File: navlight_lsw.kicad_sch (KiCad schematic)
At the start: 7 parts, among them U13 TPS26400PWP

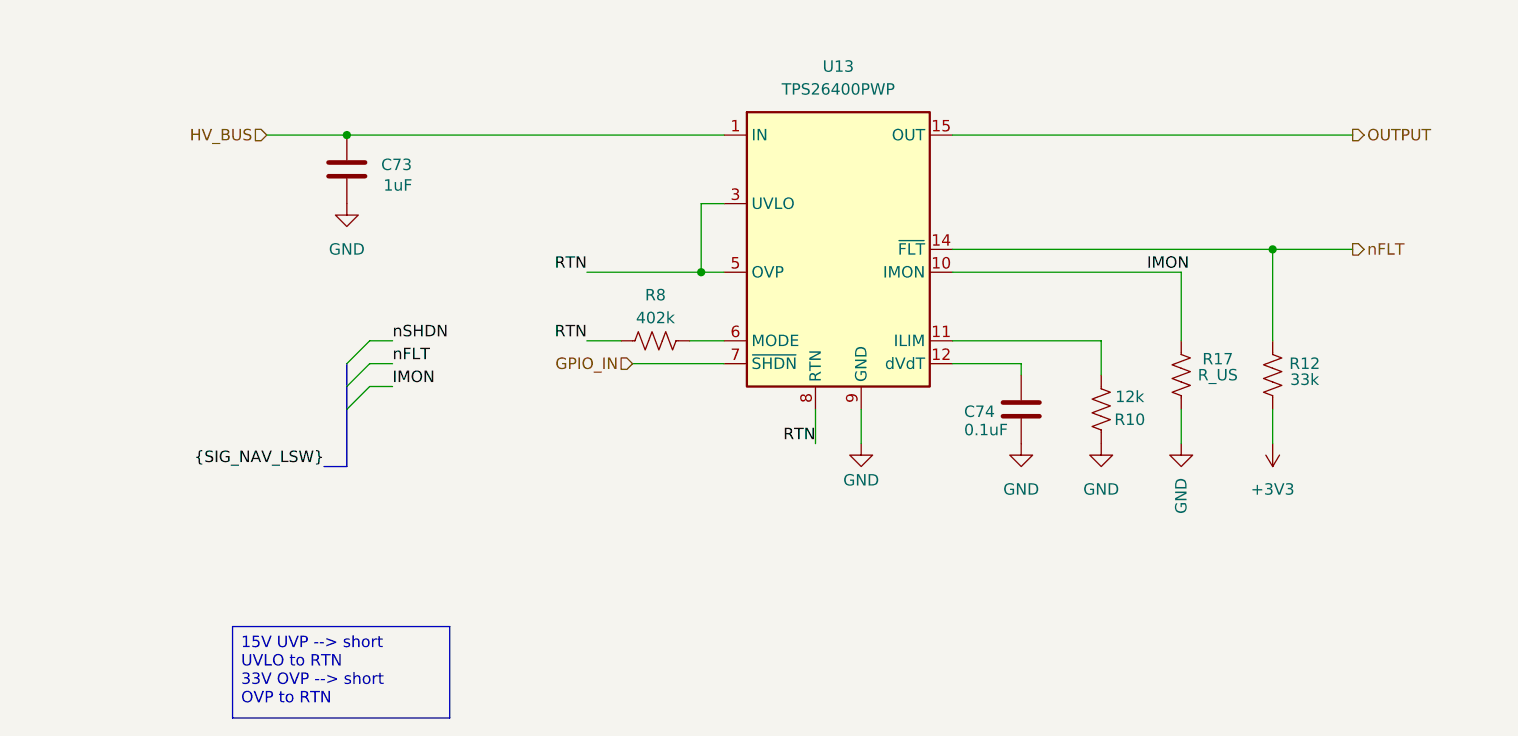
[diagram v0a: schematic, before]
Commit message: Starting bus load switch layout
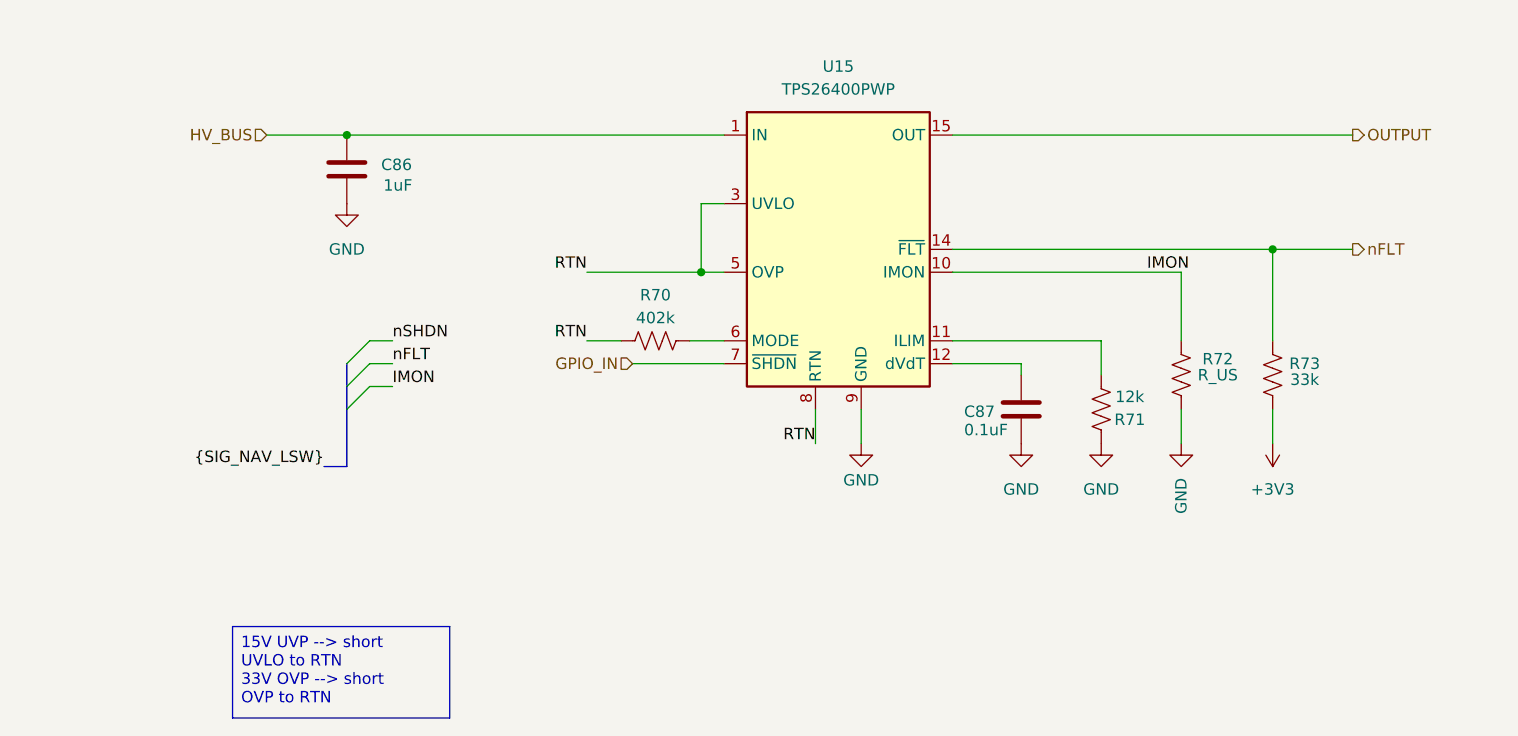
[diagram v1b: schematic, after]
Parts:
- renumbered C73 to C86, C74 to C87, R8 to R70, R10 to R71, R17 to R72, R12 to R73, U13 to U15
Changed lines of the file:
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@@
 		(on_board yes)
 		(dnp no)
-		(property "Reference" "C74"
+		(property "Reference" "C87"
 			(at 166.37 119.634 0)
 			(effects
@@
 			(project "PowerBoard"
 				(path "/99785679-20de-4827-b4cc-bc3c187068c9/9564929a-642e-4163-88c2-45054b63a5ed/a2a5e176-2ba3-4f1c-82d3-fb6903dd7d61"
-					(reference "C74")
+					(reference "C89")
 					(unit 1)
 				)
 				(path "/99785679-20de-4827-b4cc-bc3c187068c9/9564929a-642e-4163-88c2-45054b63a5ed/dd15ba19-6ae0-43ad-9da3-66d2cc4e2bc8"
-					(reference "C74")
+					(reference "C87")
 					(unit 1)
 				)
@@
 		(on_board yes)
 		(dnp no)
-		(property "Reference" "R8"
+		(property "Reference" "R70"
 			(at 132.08 106.68 90)
 			(effects
@@
 			(project ""
 				(path "/99785679-20de-4827-b4cc-bc3c187068c9/9564929a-642e-4163-88c2-45054b63a5ed/a2a5e176-2ba3-4f1c-82d3-fb6903dd7d61"
-					(reference "R9")
+					(reference "R74")
 					(unit 1)
 				)
 				(path "/99785679-20de-4827-b4cc-bc3c187068c9/9564929a-642e-4163-88c2-45054b63a5ed/dd15ba19-6ae0-43ad-9da3-66d2cc4e2bc8"
-					(reference "R8")
+					(reference "R70")
 					(unit 1)
 				)
@@
 		(dnp no)
 		(fields_autoplaced yes)
-		(property "Reference" "#PWR0120"
+		(property "Reference" "#PWR0152"
 			(at 97.79 102.87 0)
 			(effects
@@
 			(project "PowerBoard"
 				(path "/99785679-20de-4827-b4cc-bc3c187068c9/9564929a-642e-4163-88c2-45054b63a5ed/a2a5e176-2ba3-4f1c-82d3-fb6903dd7d61"
-					(reference "#PWR0120")
+					(reference "#PWR0158")
 					(unit 1)
 				)
 				(path "/99785679-20de-4827-b4cc-bc3c187068c9/9564929a-642e-4163-88c2-45054b63a5ed/dd15ba19-6ae0-43ad-9da3-66d2cc4e2bc8"
-					(reference "#PWR0120")
+					(reference "#PWR0152")
 					(unit 1)
 				)
@@
 		(dnp no)
 		(fields_autoplaced yes)
-		(property "Reference" "#PWR028"
+		(property "Reference" "#PWR0154"
 			(at 172.72 129.54 0)
 			(effects
@@
 			(project ""
 				(path "/99785679-20de-4827-b4cc-bc3c187068c9/9564929a-642e-4163-88c2-45054b63a5ed/a2a5e176-2ba3-4f1c-82d3-fb6903dd7d61"
-					(reference "#PWR029")
+					(reference "#PWR0160")
 					(unit 1)
 				)
 				(path "/99785679-20de-4827-b4cc-bc3c187068c9/9564929a-642e-4163-88c2-45054b63a5ed/dd15ba19-6ae0-43ad-9da3-66d2cc4e2bc8"
-					(reference "#PWR028")
+					(reference "#PWR0154")
 					(unit 1)
 				)
@@
 		(dnp no)
 		(fields_autoplaced yes)
-		(property "Reference" "#PWR034"
+		(property "Reference" "#PWR0157"
 			(at 200.66 119.38 0)
 			(effects
@@
 			(project ""
 				(path "/99785679-20de-4827-b4cc-bc3c187068c9/9564929a-642e-4163-88c2-45054b63a5ed/a2a5e176-2ba3-4f1c-82d3-fb6903dd7d61"
-					(reference "#PWR035")
+					(reference "#PWR0163")
 					(unit 1)
 				)
 				(path "/99785679-20de-4827-b4cc-bc3c187068c9/9564929a-642e-4163-88c2-45054b63a5ed/dd15ba19-6ae0-43ad-9da3-66d2cc4e2bc8"
-					(reference "#PWR034")
+					(reference "#PWR0157")
 					(unit 1)
 				)
@@
 		(on_board yes)
 		(dnp no)
-		(property "Reference" "C73"
+		(property "Reference" "C86"
 			(at 101.6 92.202 0)
 			(effects
@@
 			(project "PowerBoard"
 				(path "/99785679-20de-4827-b4cc-bc3c187068c9/9564929a-642e-4163-88c2-45054b63a5ed/a2a5e176-2ba3-4f1c-82d3-fb6903dd7d61"
-					(reference "C73")
+					(reference "C88")
 					(unit 1)
 				)
 				(path "/99785679-20de-4827-b4cc-bc3c187068c9/9564929a-642e-4163-88c2-45054b63a5ed/dd15ba19-6ae0-43ad-9da3-66d2cc4e2bc8"
-					(reference "C73")
+					(reference "C86")
 					(unit 1)
 				)
@@
 		(on_board yes)
 		(dnp no)
-		(property "Reference" "#PWR0121"
+		(property "Reference" "#PWR0153"
 			(at 154.94 129.54 0)
 			(effects
@@
 			(project "PowerBoard"
 				(path "/99785679-20de-4827-b4cc-bc3c187068c9/9564929a-642e-4163-88c2-45054b63a5ed/a2a5e176-2ba3-4f1c-82d3-fb6903dd7d61"
-					(reference "#PWR0121")
+					(reference "#PWR0159")
 					(unit 1)
 				)
 				(path "/99785679-20de-4827-b4cc-bc3c187068c9/9564929a-642e-4163-88c2-45054b63a5ed/dd15ba19-6ae0-43ad-9da3-66d2cc4e2bc8"
-					(reference "#PWR0121")
+					(reference "#PWR0153")
 					(unit 1)
 				)
@@
 		(dnp no)
 		(fields_autoplaced yes)
-		(property "Reference" "#PWR030"
+		(property "Reference" "#PWR0155"
 			(at 181.61 129.54 0)
 			(effects
@@
 			(project "PowerBoard"
 				(path "/99785679-20de-4827-b4cc-bc3c187068c9/9564929a-642e-4163-88c2-45054b63a5ed/a2a5e176-2ba3-4f1c-82d3-fb6903dd7d61"
-					(reference "#PWR031")
+					(reference "#PWR0161")
 					(unit 1)
 				)
 				(path "/99785679-20de-4827-b4cc-bc3c187068c9/9564929a-642e-4163-88c2-45054b63a5ed/dd15ba19-6ae0-43ad-9da3-66d2cc4e2bc8"
-					(reference "#PWR030")
+					(reference "#PWR0155")
 					(unit 1)
 				)
@@
 		(on_board yes)
 		(dnp no)
-		(property "Reference" "R17"
+		(property "Reference" "R72"
 			(at 194.564 113.792 0)
 			(effects
@@
 			(project ""
 				(path "/99785679-20de-4827-b4cc-bc3c187068c9/9564929a-642e-4163-88c2-45054b63a5ed/a2a5e176-2ba3-4f1c-82d3-fb6903dd7d61"
-					(reference "R18")
+					(reference "R76")
 					(unit 1)
 				)
 				(path "/99785679-20de-4827-b4cc-bc3c187068c9/9564929a-642e-4163-88c2-45054b63a5ed/dd15ba19-6ae0-43ad-9da3-66d2cc4e2bc8"
-					(reference "R17")
+					(reference "R72")
 					(unit 1)
 				)
@@
 		(dnp no)
 		(fields_autoplaced yes)
-		(property "Reference" "U13"
+		(property "Reference" "U15"
 			(at 152.4 81.28 0)
 			(effects
@@
 			(project "PowerBoard"
 				(path "/99785679-20de-4827-b4cc-bc3c187068c9/9564929a-642e-4163-88c2-45054b63a5ed/a2a5e176-2ba3-4f1c-82d3-fb6903dd7d61"
-					(reference "U13")
+					(reference "U16")
 					(unit 1)
 				)
 				(path "/99785679-20de-4827-b4cc-bc3c187068c9/9564929a-642e-4163-88c2-45054b63a5ed/dd15ba19-6ae0-43ad-9da3-66d2cc4e2bc8"
-					(reference "U13")
+					(reference "U15")
 					(unit 1)
 				)
@@
 		(on_board yes)
 		(dnp no)
-		(property "Reference" "R10"
+		(property "Reference" "R71"
 			(at 184.785 120.523 0)
 			(effects
@@
 			(project ""
 				(path "/99785679-20de-4827-b4cc-bc3c187068c9/9564929a-642e-4163-88c2-45054b63a5ed/a2a5e176-2ba3-4f1c-82d3-fb6903dd7d61"
-					(reference "R11")
+					(reference "R75")
 					(unit 1)
 				)
 				(path "/99785679-20de-4827-b4cc-bc3c187068c9/9564929a-642e-4163-88c2-45054b63a5ed/dd15ba19-6ae0-43ad-9da3-66d2cc4e2bc8"
-					(reference "R10")
+					(reference "R71")
 					(unit 1)
 				)
@@
 		(on_board yes)
 		(dnp no)
-		(property "Reference" "R12"
+		(property "Reference" "R73"
 			(at 204.216 114.3 0)
 			(effects
@@
 			(project "PowerBoard"
 				(path "/99785679-20de-4827-b4cc-bc3c187068c9/9564929a-642e-4163-88c2-45054b63a5ed/a2a5e176-2ba3-4f1c-82d3-fb6903dd7d61"
-					(reference "R13")
+					(reference "R77")
 					(unit 1)
 				)
 				(path "/99785679-20de-4827-b4cc-bc3c187068c9/9564929a-642e-4163-88c2-45054b63a5ed/dd15ba19-6ae0-43ad-9da3-66d2cc4e2bc8"
-					(reference "R12")
+					(reference "R73")
 					(unit 1)
 				)
@@
 		(dnp no)
 		(fields_autoplaced yes)
-		(property "Reference" "#PWR032"
+		(property "Reference" "#PWR0156"
 			(at 190.5 129.54 0)
 			(effects
@@
 			(project "PowerBoard"
 				(path "/99785679-20de-4827-b4cc-bc3c187068c9/9564929a-642e-4163-88c2-45054b63a5ed/a2a5e176-2ba3-4f1c-82d3-fb6903dd7d61"
-					(reference "#PWR033")
+					(reference "#PWR0162")
 					(unit 1)
 				)
 				(path "/99785679-20de-4827-b4cc-bc3c187068c9/9564929a-642e-4163-88c2-45054b63a5ed/dd15ba19-6ae0-43ad-9da3-66d2cc4e2bc8"
-					(reference "#PWR032")
-					(unit 1)
-				)
+					(reference "#PWR0156")
+					(unit 1)
+				)

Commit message: Working on it
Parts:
- removed R70: 402k, Resistor_SMD:R_0603_1608Metric, symbol Device:R_US
- removed R71: 12k, Resistor_SMD:R_0603_1608Metric, symbol Device:R_US
- removed R72: R_US, Resistor_SMD:R_0603_1608Metric, symbol Device:R_US
- removed R73: 33k, Resistor_SMD:R_0603_1608Metric, symbol Device:R_US
- removed U15: TPS26400PWP, Package_DFN_QFN:VQFN-24-1EP_4x4mm_P0.5mm_EP2.45x2.45mm_ThermalVias, symbol Power_Management:TPS26400PWP
- added R66: 402k, Resistor_SMD:R_0603_1608Metric, symbol Device:R_US
- added R67: 33k, Resistor_SMD:R_0603_1608Metric, symbol Device:R_US
- added R68, R69: 12k, Resistor_SMD:R_0603_1608Metric, symbol Device:R_US
- added U15: TPS26400RHFR, _PowerBoard:RHF0024A-MFG, symbol _TPS26400RHFR:TPS26400RHFR
- C87: Supplier_2 (none) -> JLCPCB; Supplier_2_Price @ QTY (none) -> 1
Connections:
- net +3V3: now also R67.1
- net GND: now also U15.17 (GND); no longer C87.2
- net GPIO_IN: now also U15.14 (SHDN_N)
- net HV_BUS: now also U15.8 (IN), U15.9 (IN)
- net OUTPUT: now also U15.23 (OUT), U15.24 (OUT)
- net RTN: now also C87.1, R66.1, R68.1, R69.1, U15.10 (UVLO), U15.12 (OVP), U15.15 (RTN), U15.25 (PowerPAD)
- net nFLT: now also R67.2, U15.22 (FLT_N)
- new net: R69.2, U15.19 (ILIM)
- new net: R66.2, U15.13 (MODE)
- new net: C87.2, U15.20 (dVdT)
- new net: R68.2, U15.18 (IMON)
- no-connect marks 0 -> 10

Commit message: Working on schematic and layout
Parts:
- renumbered R66 to R67, R67 to R68, R68 to R69, R69 to R70, U15 to U16
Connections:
- net GPIO_IN is gone; now on net nSHDN: U16.14 (SHDN_N)
- net IMON: now also R69.2, U16.18 (IMON)
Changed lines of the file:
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@@
+		)
+	)
+	(label "nSHDN"
+		(at 193.04 102.87 0)
+		(effects
+			(font
+				(size 1.27 1.27)
+			)
+			(justify left bottom)
+		)
+	)
+	(label "IMON"
+		(at 172.72 107.95 0)
+		(effects
+			(font
+				(size 1.27 1.27)
+			)
+			(justify left bottom)
 		)
 	)
@@
 		)
 	)
+	(label "nFLT"
+		(at 175.26 93.98 0)
+		(effects
+			(font
+				(size 1.27 1.27)
+			)
+			(justify left bottom)
+		)
+	)
 	(label "nSHDN"
 		(at 87.63 111.76 0)
@@
 			)
 			(justify left bottom)
-		)
-	)
-	(label "{SIG_NAV_LSW}"
-		(at 80.01 125.73 180)
-		(effects
-			(font
-				(size 1.27 1.27)
-			)
-			(justify right bottom)
 		)
 	)
@@
 		)
 	)
-	(hierarchical_label "GPIO_IN"
-		(shape input)
-		(at 193.04 102.87 0)
+	(hierarchical_label "{SIG_NAV_LSW}"
+		(shape bidirectional)
+		(at 80.01 125.73 180)
 		(effects
 			(font
 				(size 1.27 1.27)
 			)
-			(justify left)
-		)
-	)
-	(hierarchical_label "nFLT"
-		(shape output)
-		(at 175.26 93.98 0)
-		(effects
-			(font
-				(size 1.27 1.27)
-			)
-			(justify left)
+			(justify right)
 		)
 	)
@@
 		(on_board yes)
 		(dnp no)
-		(property "Reference" "R69"
-			(at 181.61 108.712 90)
+		(property "Reference" "R70"
+			(at 181.61 109.728 90)
 			(effects
 				(font
@@
 			(project "PowerBoard"
 				(path "/99785679-20de-4827-b4cc-bc3c187068c9/9564929a-642e-4163-88c2-45054b63a5ed/a2a5e176-2ba3-4f1c-82d3-fb6903dd7d61"
-					(reference "R73")
+					(reference "R74")
 					(unit 1)
 				)
 				(path "/99785679-20de-4827-b4cc-bc3c187068c9/9564929a-642e-4163-88c2-45054b63a5ed/dd15ba19-6ae0-43ad-9da3-66d2cc4e2bc8"
-					(reference "R69")
+					(reference "R70")
 					(unit 1)
 				)
@@
 		(on_board yes)
 		(dnp no)
-		(property "Reference" "R66"
+		(property "Reference" "R67"
 			(at 119.38 102.87 90)
 			(effects
@@
 			(project "PowerBoard"
 				(path "/99785679-20de-4827-b4cc-bc3c187068c9/9564929a-642e-4163-88c2-45054b63a5ed/a2a5e176-2ba3-4f1c-82d3-fb6903dd7d61"
-					(reference "R70")
+					(reference "R71")
 					(unit 1)
 				)
 				(path "/99785679-20de-4827-b4cc-bc3c187068c9/9564929a-642e-4163-88c2-45054b63a5ed/dd15ba19-6ae0-43ad-9da3-66d2cc4e2bc8"
-					(reference "R66")
+					(reference "R67")
 					(unit 1)
 				)
@@
 		(on_board yes)
 		(dnp no)
-		(property "Reference" "R67"
+		(property "Reference" "R68"
 			(at 185.42 94.742 90)
 			(effects
@@
 			(project "PowerBoard"
 				(path "/99785679-20de-4827-b4cc-bc3c187068c9/9564929a-642e-4163-88c2-45054b63a5ed/a2a5e176-2ba3-4f1c-82d3-fb6903dd7d61"
-					(reference "R71")
+					(reference "R72")
 					(unit 1)
 				)
 				(path "/99785679-20de-4827-b4cc-bc3c187068c9/9564929a-642e-4163-88c2-45054b63a5ed/dd15ba19-6ae0-43ad-9da3-66d2cc4e2bc8"
-					(reference "R67")
+					(reference "R68")
 					(unit 1)
 				)
@@
 		(dnp no)
 		(fields_autoplaced yes)
-		(property "Reference" "#PWR0152"
+		(property "Reference" "#PWR0155"
 			(at 82.55 101.6 0)
 			(effects
@@
 			(project "PowerBoard"
 				(path "/99785679-20de-4827-b4cc-bc3c187068c9/9564929a-642e-4163-88c2-45054b63a5ed/a2a5e176-2ba3-4f1c-82d3-fb6903dd7d61"
+					(reference "#PWR0158")
+					(unit 1)
+				)
+				(path "/99785679-20de-4827-b4cc-bc3c187068c9/9564929a-642e-4163-88c2-45054b63a5ed/dd15ba19-6ae0-43ad-9da3-66d2cc4e2bc8"
 					(reference "#PWR0155")
-					(unit 1)
-				)
-				(path "/99785679-20de-4827-b4cc-bc3c187068c9/9564929a-642e-4163-88c2-45054b63a5ed/dd15ba19-6ae0-43ad-9da3-66d2cc4e2bc8"
-					(reference "#PWR0152")
 					(unit 1)
 				)
@@
 		(on_board yes)
 		(dnp no)
-		(property "Reference" "#PWR0153"
+		(property "Reference" "#PWR0156"
 			(at 177.8 133.35 0)
 			(effects
@@
 			(project "PowerBoard"
 				(path "/99785679-20de-4827-b4cc-bc3c187068c9/9564929a-642e-4163-88c2-45054b63a5ed/a2a5e176-2ba3-4f1c-82d3-fb6903dd7d61"
+					(reference "#PWR0159")
+					(unit 1)
+				)
+				(path "/99785679-20de-4827-b4cc-bc3c187068c9/9564929a-642e-4163-88c2-45054b63a5ed/dd15ba19-6ae0-43ad-9da3-66d2cc4e2bc8"
 					(reference "#PWR0156")
-					(unit 1)
-				)
-				(path "/99785679-20de-4827-b4cc-bc3c187068c9/9564929a-642e-4163-88c2-45054b63a5ed/dd15ba19-6ae0-43ad-9da3-66d2cc4e2bc8"
-					(reference "#PWR0153")
 					(unit 1)
 				)
@@
 		(dnp no)
 		(fields_autoplaced yes)
-		(property "Reference" "U15"
+		(property "Reference" "U16"
 			(at 151.13 77.47 0)
 			(effects
@@
 			(project ""
 				(path "/99785679-20de-4827-b4cc-bc3c187068c9/9564929a-642e-4163-88c2-45054b63a5ed/a2a5e176-2ba3-4f1c-82d3-fb6903dd7d61"
+					(reference "U17")
+					(unit 1)
+				)
+				(path "/99785679-20de-4827-b4cc-bc3c187068c9/9564929a-642e-4163-88c2-45054b63a5ed/dd15ba19-6ae0-43ad-9da3-66d2cc4e2bc8"
 					(reference "U16")
-					(unit 1)
-				)
-				(path "/99785679-20de-4827-b4cc-bc3c187068c9/9564929a-642e-4163-88c2-45054b63a5ed/dd15ba19-6ae0-43ad-9da3-66d2cc4e2bc8"
-					(reference "U15")
 					(unit 1)
 				)
@@
 		(on_board yes)
 		(dnp no)
-		(property "Reference" "R68"
-			(at 181.61 103.632 90)
+		(property "Reference" "R69"
+			(at 181.61 103.886 90)
 			(effects
 				(font
@@
 		)
 		(property "Value" "12k"
-			(at 181.61 106.172 90)
+			(at 181.61 105.664 90)
 			(effects
 				(font
@@
 			(project "PowerBoard"
 				(path "/99785679-20de-4827-b4cc-bc3c187068c9/9564929a-642e-4163-88c2-45054b63a5ed/a2a5e176-2ba3-4f1c-82d3-fb6903dd7d61"
-					(reference "R72")
+					(reference "R73")
 					(unit 1)
 				)
 				(path "/99785679-20de-4827-b4cc-bc3c187068c9/9564929a-642e-4163-88c2-45054b63a5ed/dd15ba19-6ae0-43ad-9da3-66d2cc4e2bc8"
-					(reference "R68")
+					(reference "R69")
 					(unit 1)
 				)
@@
 		(on_board yes)
 		(dnp no)
-		(fields_autoplaced yes)
-		(property "Reference" "#PWR0154"
+		(property "Reference" "#PWR0157"
 			(at 185.42 97.79 0)
 			(effects
@@
 		)
 		(property "Value" "+3V3"
-			(at 194.31 97.79 0)
+			(at 195.072 97.536 90)
 			(effects
 				(font
@@
 			(project "PowerBoard"
 				(path "/99785679-20de-4827-b4cc-bc3c187068c9/9564929a-642e-4163-88c2-45054b63a5ed/a2a5e176-2ba3-4f1c-82d3-fb6903dd7d61"
+					(reference "#PWR0160")
+					(unit 1)
+				)
+				(path "/99785679-20de-4827-b4cc-bc3c187068c9/9564929a-642e-4163-88c2-45054b63a5ed/dd15ba19-6ae0-43ad-9da3-66d2cc4e2bc8"
 					(reference "#PWR0157")
 					(unit 1)
 				)
-				(path "/99785679-20de-4827-b4cc-bc3c187068c9/9564929a-642e-4163-88c2-45054b63a5ed/dd15ba19-6ae0-43ad-9da3-66d2cc4e2bc8"
-					(reference "#PWR0154")
-					(unit 1)
-				)
